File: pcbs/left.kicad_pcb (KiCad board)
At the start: 2 copper layers, 125.1 x 95.2 mm, 27 parts

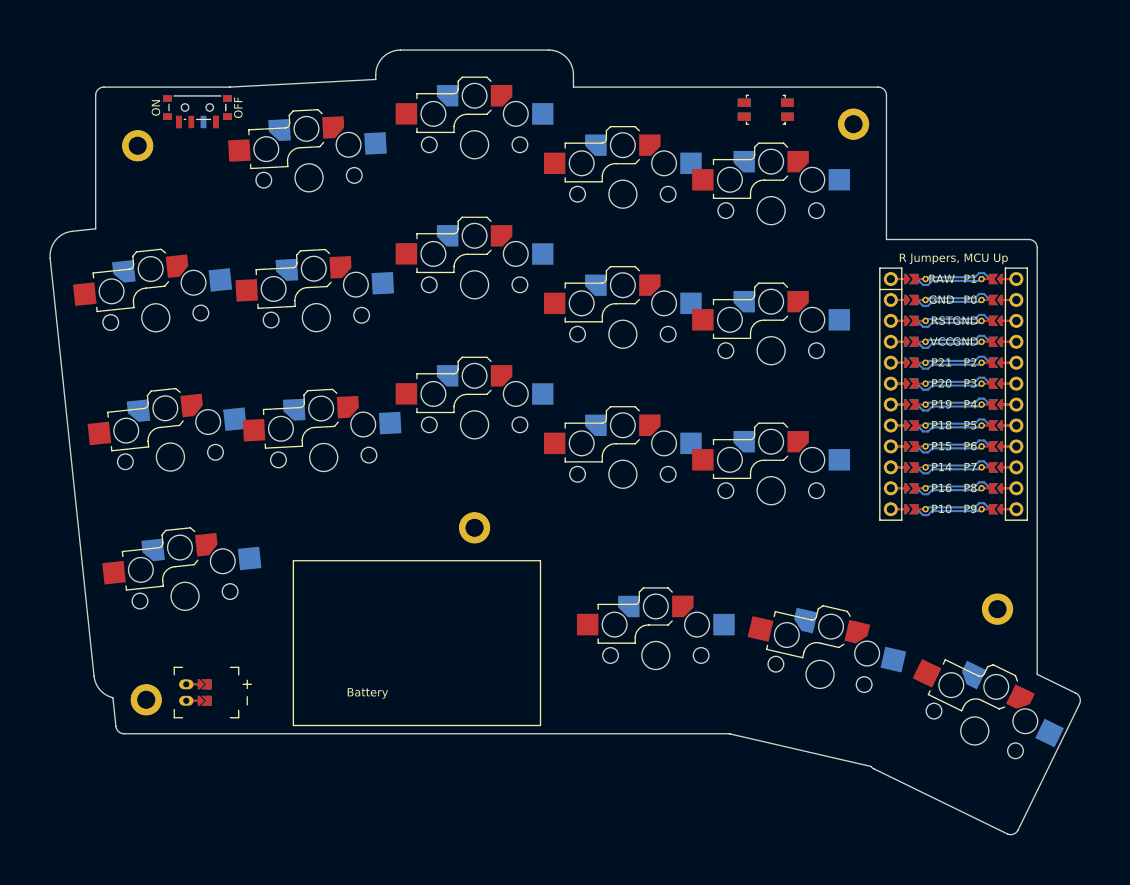
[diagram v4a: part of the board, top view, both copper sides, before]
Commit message: Remove temporary expands and move power switch slightly away from the edge
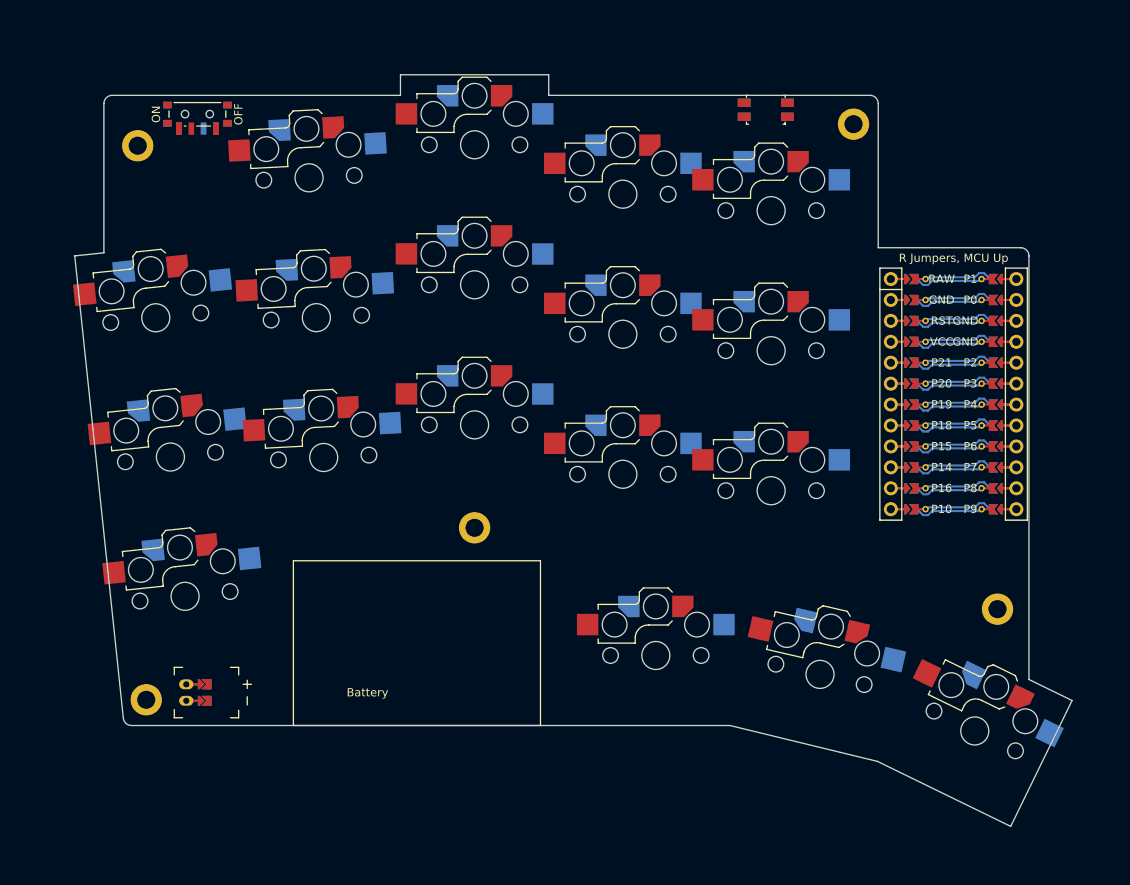
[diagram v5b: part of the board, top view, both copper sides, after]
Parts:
- moved PWR1 0.80 mm to (101.5, 41.5)
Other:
- board size 125.1 x 95.2 mm -> 121.1 x 91.2 mm
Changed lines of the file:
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@@
   (footprint "ceoloide:power_switch_smd_side"
     (layer "F.Cu")
-    (at 101.49836669999999 40.68429119999999 90)
+    (at 101.49836669999999 41.48429119999999 90)
     (property "Reference" "PWR1"
       (at -3.6 0 0)
@@
     )
   )
-  (gr_line (start 147.1483666 38.18429119999999) (end 147.1483667 36.68429119999999) (layer Edge.Cuts) (stroke (width 0.15) (type default)))
-(gr_arc (start 147.1483667 36.68429119999999) (mid 146.269687 34.56297079999999) (end 144.1483667 33.68429119999999) (layer Edge.Cuts) (stroke (width 0.15) (type default)))
-(gr_line (start 144.1483667 33.68429119999999) (end 126.1483667 33.68429119999999) (layer Edge.Cuts) (stroke (width 0.15) (type default)))
-(gr_arc (start 126.1483667 33.68429119999999) (mid 124.0270464 34.56297089999999) (end 123.1483667 36.68429119999999) (layer Edge.Cuts) (stroke (width 0.15) (type default)))
-(gr_line (start 123.1483667 36.68429119999999) (end 123.1483667 37.25485987602707) (layer Edge.Cuts) (stroke (width 0.15) (type default)))
-(gr_line (start 123.1483667 37.25485987602707) (end 105.4622228 38.1817515) (layer Edge.Cuts) (stroke (width 0.15) (type default)))
-(gr_arc (start 105.4617762 38.1817748) (mid 105.4406227 38.1829583) (end 105.41947809999999 38.1842912) (layer Edge.Cuts) (stroke (width 0.15) (type default)))
-(gr_line (start 89.1483667 55.3899259419181) (end 86.29325769999998 55.69001000000001) (layer Edge.Cuts) (stroke (width 0.15) (type default)))
-(gr_arc (start 86.29325779999999 55.69001000000001) (mid 84.27540529999999 56.78561460000001) (end 83.62327749999999 58.98716120000001) (layer Edge.Cuts) (stroke (width 0.15) (type default)))
-(gr_line (start 83.6232775 58.98716120000001) (end 88.9542292 109.7077778) (layer Edge.Cuts) (stroke (width 0.15) (type default)))
-(gr_arc (start 88.9542292 109.7077778) (mid 89.6827724 111.3727962) (end 91.2389242 112.3116535) (layer Edge.Cuts) (stroke (width 0.15) (type default)))
-(gr_line (start 92.5989109 116.68429119999999) (end 166.0842466 116.68429119999999) (layer Edge.Cuts) (stroke (width 0.15) (type default)))
-(gr_arc (start 166.0842466 116.68429119999999) (mid 166.12960690000003 116.6982274) (end 166.17557730000001 116.70999599999999) (layer Edge.Cuts) (stroke (width 0.15) (type default)))
-(gr_line (start 166.17557730000001 116.70999599999999) (end 183.2648105 120.6553563) (layer Edge.Cuts) (stroke (width 0.15) (type default)))
-(gr_arc (start 183.2648105 120.6553563) (mid 183.4234888 120.81681569999999) (end 183.6144175 120.93844709999999) (layer Edge.Cuts) (stroke (width 0.15) (type default)))
-(gr_line (start 183.61481949999998 120.9386431) (end 199.79230840000002 128.8289316) (layer Edge.Cuts) (stroke (width 0.15) (type default)))
-(gr_arc (start 199.7927104 128.8291277) (mid 200.5566497 128.8758522) (end 201.12987550000003 128.3687048) (layer Edge.Cuts) (stroke (width 0.15) (type default)))
-(gr_line (start 201.1300715 128.36830279999998) (end 208.5819889 113.089608) (layer Edge.Cuts) (stroke (width 0.15) (type default)))
-(gr_arc (start 208.58218500000004 113.08920599999999) (mid 208.62890950000002 112.32526669999999) (end 208.12176210000004 111.7520409) (layer Edge.Cuts) (stroke (width 0.15) (type default)))
-(gr_line (start 208.12136010000003 111.7518449) (end 203.4483666 109.4726736947813) (layer Edge.Cuts) (stroke (width 0.15) (type default)))
-(gr_line (start 185.1483667 56.684291099999996) (end 202.4483666 56.684291099999996) (layer Edge.Cuts) (stroke (width 0.15) (type default)))
-(gr_arc (start 203.4483666 57.684291099999996) (mid 203.1554734 56.9771843) (end 202.4483666 56.684291099999996) (layer Edge.Cuts) (stroke (width 0.15) (type default)))
-(gr_line (start 203.4483666 57.684291099999996) (end 203.4483666 109.4726736947813) (layer Edge.Cuts) (stroke (width 0.15) (type default)))
-(gr_line (start 91.60438903481348 115.78881969999996) (end 91.2389242 112.3116535) (layer Edge.Cuts) (stroke (width 0.15) (type default)))
-(gr_arc (start 91.60438903481348 115.78881969999996) (mid 91.92978033481347 116.42743599999996) (end 92.59891093481347 116.68429119999996) (layer Edge.Cuts) (stroke (width 0.15) (type default)))
-(gr_line (start 89.1483667 55.3899259419181) (end 89.1483667 39.18429119999999) (layer Edge.Cuts) (stroke (width 0.15) (type default)))
-(gr_arc (start 90.1483667 38.18429119999999) (mid 89.44125989999999 38.47718439999999) (end 89.1483667 39.18429119999999) (layer Edge.Cuts) (stroke (width 0.15) (type default)))
-(gr_line (start 90.1483667 38.18429119999999) (end 105.41947809999999 38.1842912) (layer Edge.Cuts) (stroke (width 0.15) (type default)))
-(gr_line (start 147.1483666 38.18429119999999) (end 184.1483667 38.18429119999999) (layer Edge.Cuts) (stroke (width 0.15) (type default)))
-(gr_arc (start 185.1483667 39.18429119999999) (mid 184.8554735 38.47718439999999) (end 184.1483667 38.18429119999999) (layer Edge.Cuts) (stroke (width 0.15) (type default)))
-(gr_line (start 185.1483667 39.18429119999999) (end 185.1483667 56.684291099999996) (layer Edge.Cuts) (stroke (width 0.15) (type default)))
+  (gr_line (start 86.60684319999999 58.67357570000001) (end 92.50479308505149 114.78881969999998) (layer Edge.Cuts) (stroke (width 0.15) (type default)))
+(gr_line (start 86.60684319999999 58.67357570000001) (end 90.1483667 58.30134658019551) (layer Edge.Cuts) (stroke (width 0.15) (type default)))
+(gr_line (start 144.1483666 39.18429119999999) (end 144.1483667 36.68429119999999) (layer Edge.Cuts) (stroke (width 0.15) (type default)))
+(gr_line (start 144.1483667 36.68429119999999) (end 126.1483667 36.68429119999999) (layer Edge.Cuts) (stroke (width 0.15) (type default)))
+(gr_line (start 126.1483667 36.68429119999999) (end 126.1483667 39.18429119999999) (layer Edge.Cuts) (stroke (width 0.15) (type default)))
+(gr_line (start 93.49931498505148 115.68429119999999) (end 166.1483666 115.68429119999999) (layer Edge.Cuts) (stroke (width 0.15) (type default)))
+(gr_line (start 184.0527886 120.0396531) (end 200.23108150000002 127.93033369999999) (layer Edge.Cuts) (stroke (width 0.15) (type default)))
+(gr_line (start 200.23108150000002 127.93033369999999) (end 207.683391 112.65083489999999) (layer Edge.Cuts) (stroke (width 0.15) (type default)))
+(gr_line (start 207.683391 112.65083489999999) (end 202.4483666 110.09754292235218) (layer Edge.Cuts) (stroke (width 0.15) (type default)))
+(gr_line (start 184.0527886 120.0396531) (end 166.1483666 115.68429119999999) (layer Edge.Cuts) (stroke (width 0.15) (type default)))
+(gr_line (start 184.1483667 57.684291099999996) (end 201.4483666 57.684291099999996) (layer Edge.Cuts) (stroke (width 0.15) (type default)))
+(gr_line (start 202.4483666 110.09754292235218) (end 202.4483666 58.684291099999996) (layer Edge.Cuts) (stroke (width 0.15) (type default)))
+(gr_arc (start 202.4483666 58.684291099999996) (mid 202.1554734 57.9771843) (end 201.4483666 57.684291099999996) (layer Edge.Cuts) (stroke (width 0.15) (type default)))
+(gr_arc (start 92.50479308505149 114.78881969999996) (mid 92.83018438505148 115.42743599999996) (end 93.49931498505148 115.68429119999996) (layer Edge.Cuts) (stroke (width 0.15) (type default)))
+(gr_line (start 90.1483667 58.30134658019551) (end 90.1483667 40.18429119999999) (layer Edge.Cuts) (stroke (width 0.15) (type default)))
+(gr_line (start 91.1483667 39.18429119999999) (end 126.1483667 39.18429119999999) (layer Edge.Cuts) (stroke (width 0.15) (type default)))
+(gr_line (start 144.1483666 39.18429119999999) (end 183.1483667 39.18429119999999) (layer Edge.Cuts) (stroke (width 0.15) (type default)))
+(gr_line (start 184.1483667 40.18429119999999) (end 184.1483667 57.684291099999996) (layer Edge.Cuts) (stroke (width 0.15) (type default)))
+(gr_arc (start 91.1483667 39.18429119999999) (mid 90.44125989999999 39.47718439999999) (end 90.1483667 40.18429119999999) (layer Edge.Cuts) (stroke (width 0.15) (type default)))
+(gr_arc (start 184.1483667 40.18429119999999) (mid 183.8554735 39.47718439999999) (end 183.1483667 39.18429119999999) (layer Edge.Cuts) (stroke (width 0.15) (type default)))
 (gr_line (start 113.1483666 95.68429119999999) (end 113.1483666 115.68429119999999) (layer F.SilkS) (stroke (width 0.15) (type default)))
 (gr_line (start 113.1483666 115.68429119999999) (end 143.1483666 115.68429119999999) (layer F.SilkS) (stroke (width 0.15) (type default)))
